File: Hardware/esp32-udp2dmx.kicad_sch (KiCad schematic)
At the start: 16 parts, among them J1 Conn_01x04, J2 J1B1211CCD, P1 USB_C_Plug_USB2.0, Q1 2N7002, Q2 2N7002, U1 ESP32-S3-MINI-1U, U2 W5500, U4 MAX13487

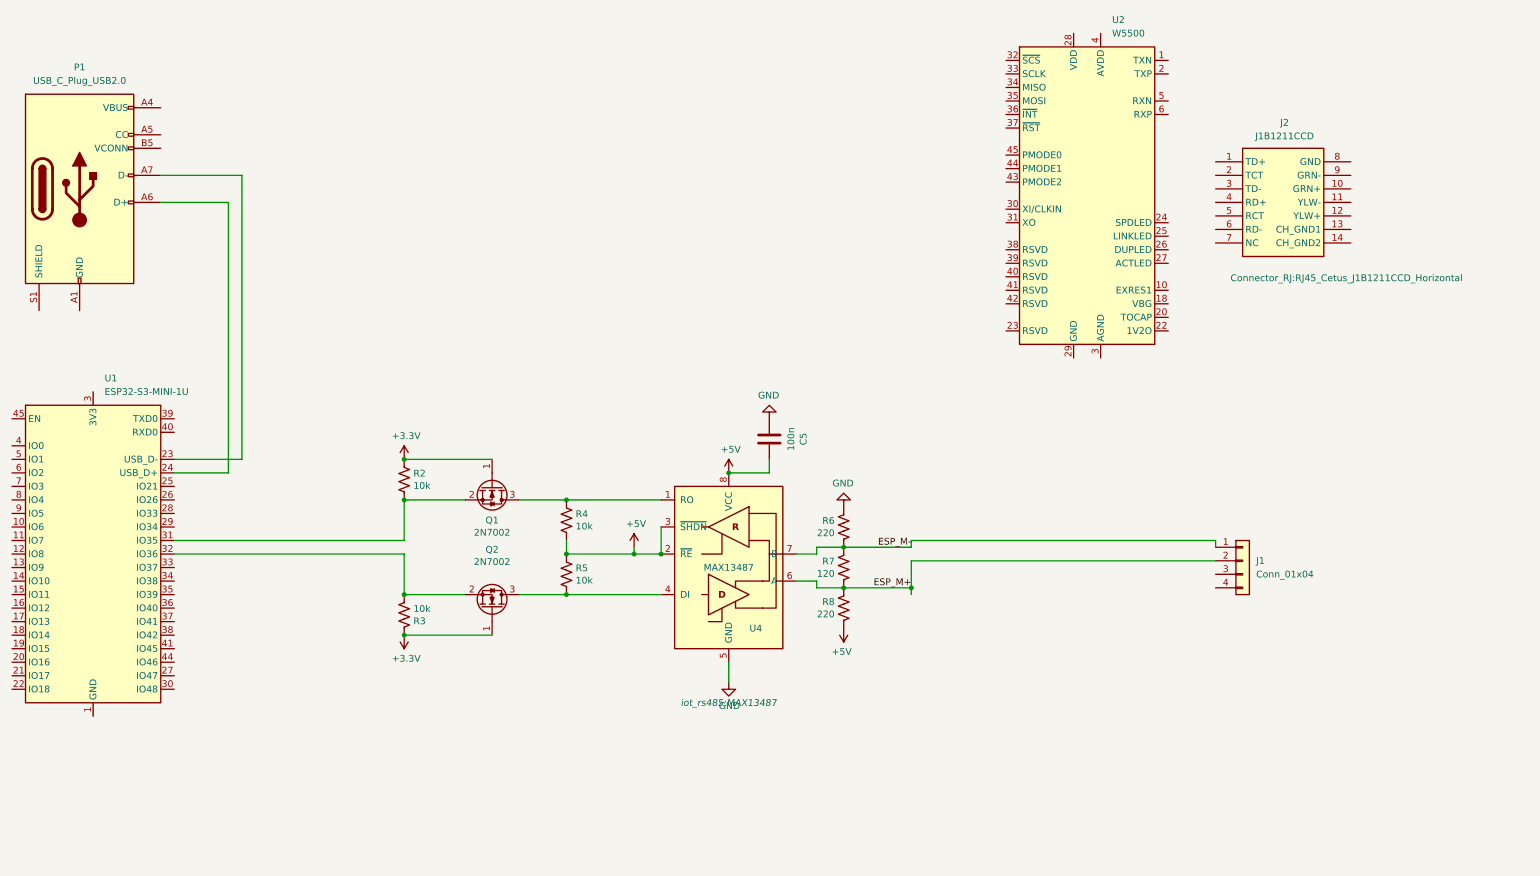
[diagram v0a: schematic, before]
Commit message: update schematic
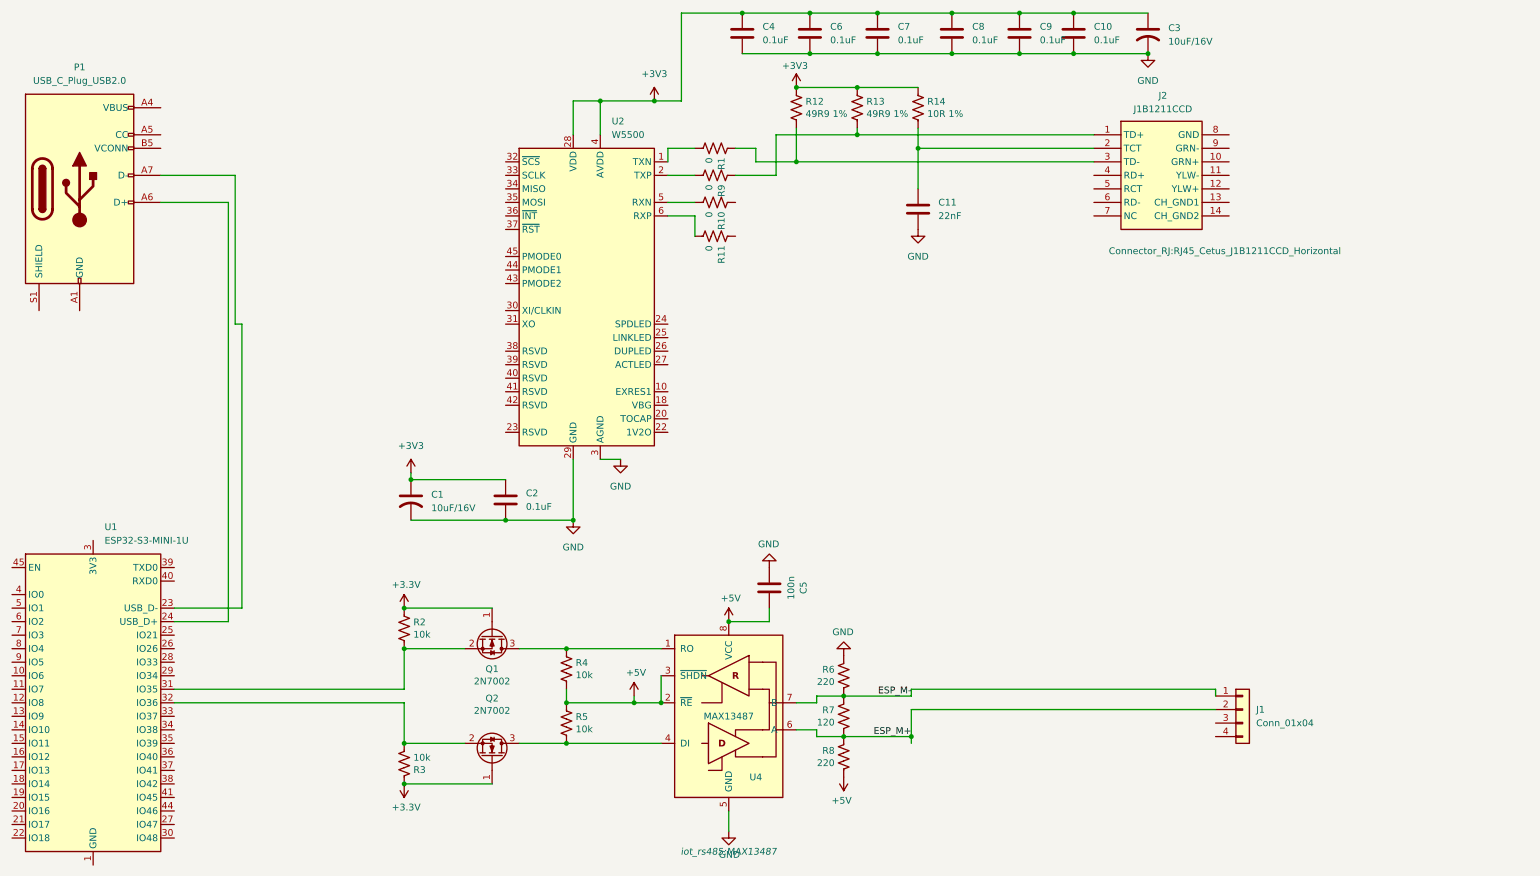
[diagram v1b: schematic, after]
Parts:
- added C1, C3: 10uF/16V, Capacitor_SMD:C_0201_0603Metric, symbol Device:C_US
- added C10, C2, C4, C6, C7, C8, C9: 0.1uF, Capacitor_SMD:C_0201_0603Metric, symbol Device:C
- added C11: 22nF, Capacitor_SMD:C_0201_0603Metric, symbol Device:C
- added R1, R10, R11, R9: 0, Resistor_SMD:R_0603_1608Metric, symbol Device:R_US
- added R12, R13: 49R9 1%, Resistor_SMD:R_0603_1608Metric, symbol Device:R_US
- added R14: 10R 1%, Resistor_SMD:R_0603_1608Metric, symbol Device:R_US
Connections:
- net GND: now also U2.14 (AGND), U2.16 (AGND), U2.19 (AGND), U2.29 (GND), U2.3 (AGND), U2.48 (AGND), U2.9 (AGND), C1.2, C10.2, C11.2, C2.2, C3.2, C4.2, C6.2, C7.2, C8.2, C9.2
- net at J2.1 (TD+): now also R13.2, R9.1
- net at J2.2 (TCT): now also C11.1, R14.2
- net at J2.3 (TD-): now also R1.1, R12.2
- net at U2.1 (TXN): now also R1.2
- net +3V3: now reaches U2.11 (AVDD), U2.15 (AVDD), U2.17 (AVDD), U2.21 (AVDD), U2.4 (AVDD), U2.8 (AVDD)
- net +3V3: now also U2.28 (VDD), C1.1, C10.1, C2.1, C3.1, C4.1, C6.1, C7.1, C8.1, C9.1, R12.1, R13.1, R14.1
- net at U2.2 (TXP): now also R9.2
- net at U2.5 (RXN): now also R10.2
- net at U2.6 (RXP): now also R11.2
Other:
- moved on the sheet: C5, J1, J2, Q1, Q2, R2, R3, R4, R5, R6, R7, R8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

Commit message: update
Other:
- note added: "https://docs.wiznet.io/Product/iEthernet/W5500/ref-schematic"
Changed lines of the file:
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@@
 	(generator_version "9.0")
 	(paper "A4")
+	(text "https://docs.wiznet.io/Product/iEthernet/W5500/ref-schematic"
+		(exclude_from_sim no)
+		(at 251.46 114.046 0)
+		(effects
+			(font
+				(size 1.27 1.27)
+			)
+		)
+	)
 	(junction
 		(at 140.97 110.49)
